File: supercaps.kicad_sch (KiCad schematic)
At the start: 21 parts, among them J30 XT30_F, J31 XT30_F, Q10 2SCR587D3, Q11 2SAR587D3, U18 TLV9301xDBV

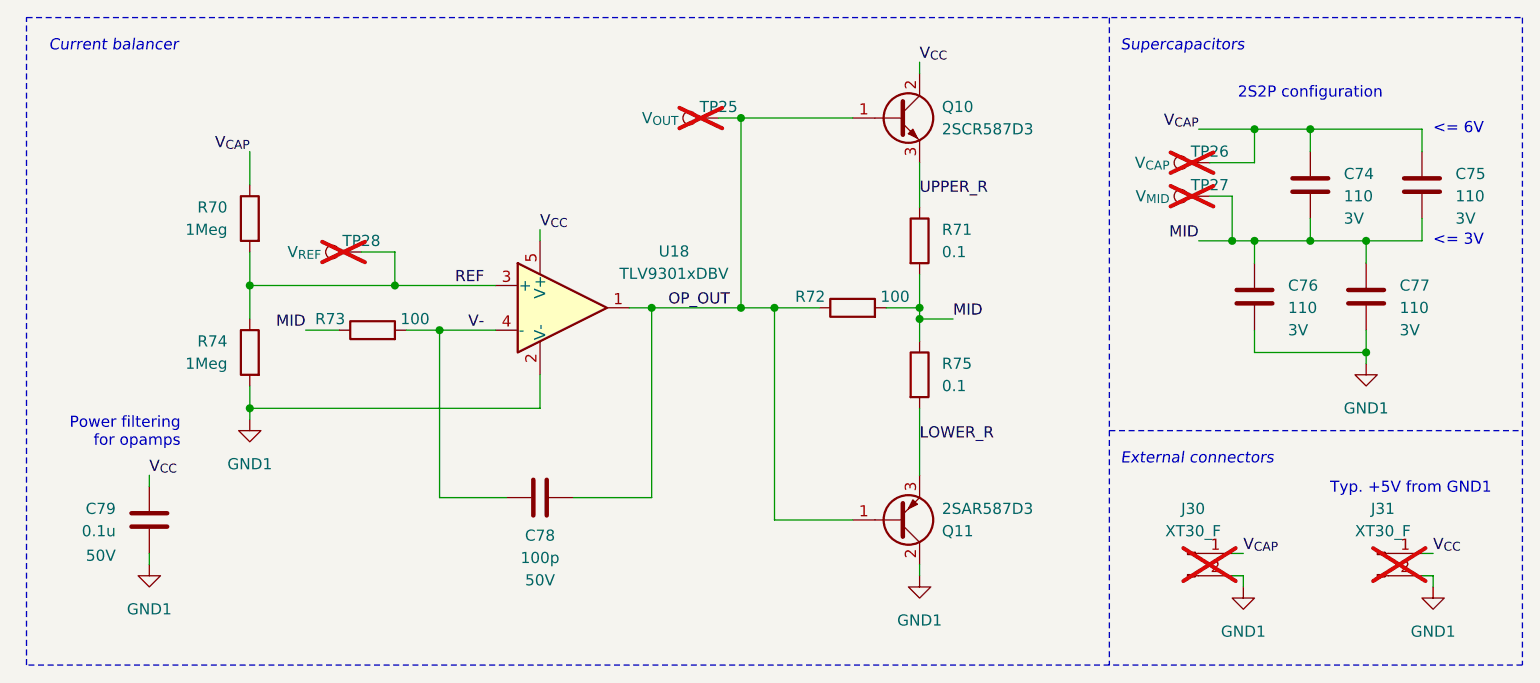
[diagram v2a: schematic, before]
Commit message: Begin layout
Completed ideal diode layout
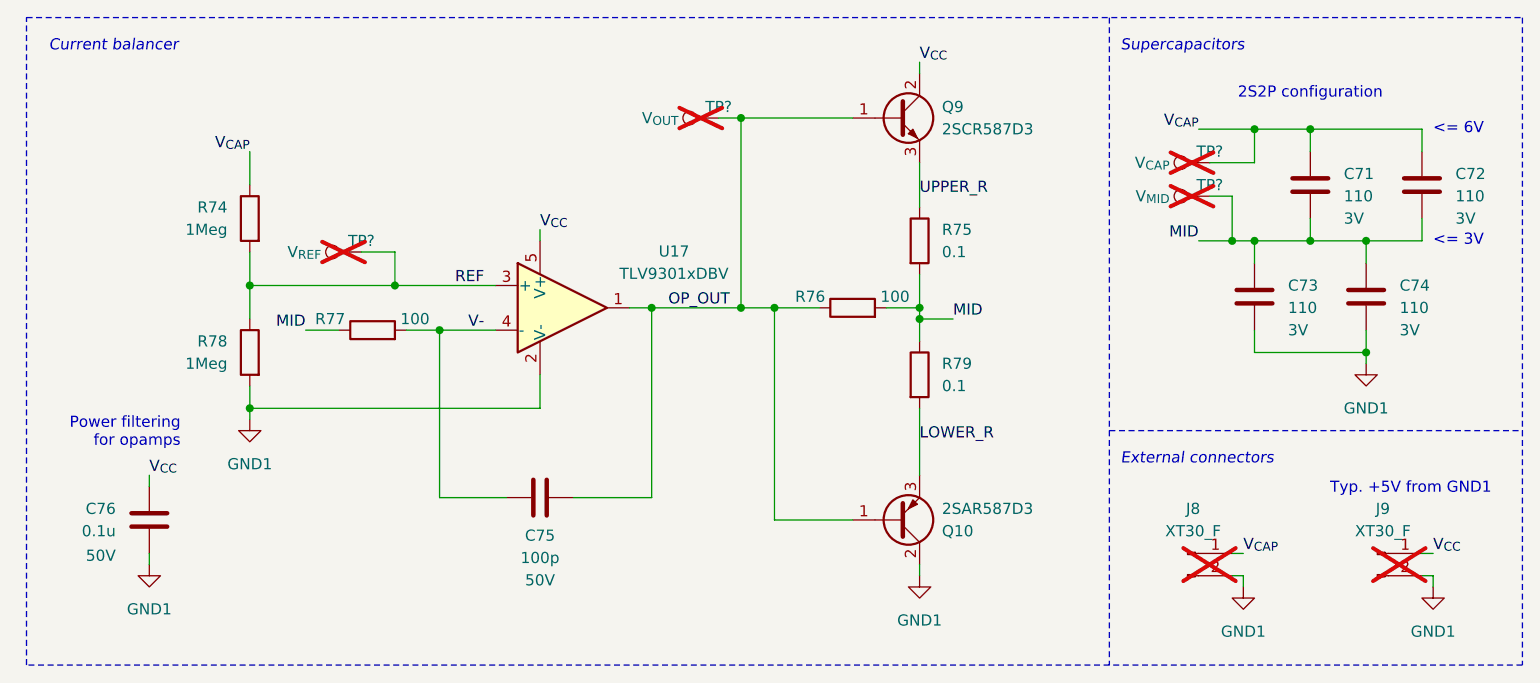
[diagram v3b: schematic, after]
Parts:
- renumbered C74 to C71, C75 to C72, C76 to C73, C77 to C74, C78 to C75, C79 to C76, J30 to J8, J31 to J9, Q11 to Q10, Q10 to Q9, R70 to R74, R71 to R75, R72 to R76, R73 to R77, R74 to R78, R75 to R79, TP28 to TP?, TP25 to TP?, TP26 to TP?, TP27 to TP?, U18 to U17
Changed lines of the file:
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@@
 		(on_board yes)
 		(dnp yes)
-		(property "Reference" "TP28"
+		(property "Reference" "TP?"
 			(at 59.69 50.8 90)
 			(effects
@@
 		)
 		(instances
+			(project "SupercapManager"
+				(path "/6197145b-e7d4-44cc-9d90-537b6501bf60/e69614f9-5cd8-4aa3-ae42-53f80cb78886"
+					(reference "TP?")
+					(unit 1)
+				)
+			)
 			(project "Rev 1B"
 				(path "/e5f99deb-ef42-4c5f-b80a-388477910e20/1165d5b5-e274-4083-890a-7a12aee56ddf"
@@
 		(on_board yes)
 		(dnp no)
-		(property "Reference" "R75"
+		(property "Reference" "R79"
 			(at 125.73 64.7699 0)
 			(effects
@@
 		(on_board yes)
 		(dnp no)
-		(property "Reference" "U18"
+		(property "Reference" "U17"
 			(at 95.25 51.9998 0)
 			(effects
@@
 		(on_board yes)
 		(dnp yes)
-		(property "Reference" "TP25"
+		(property "Reference" "TP?"
 			(at 100.33 35.56 90)
 			(effects
@@
 		)
 		(instances
+			(project "SupercapManager"
+				(path "/6197145b-e7d4-44cc-9d90-537b6501bf60/e69614f9-5cd8-4aa3-ae42-53f80cb78886"
+					(reference "TP?")
+					(unit 1)
+				)
+			)
 			(project "Rev 1B"
 				(path "/e5f99deb-ef42-4c5f-b80a-388477910e20/1165d5b5-e274-4083-890a-7a12aee56ddf"
@@
 		(on_board yes)
 		(dnp no)
-		(property "Reference" "C78"
+		(property "Reference" "C75"
 			(at 80.01 84.328 90)
 			(effects
@@
 		(exclude_from_sim no)
 		(in_bom yes)
-		(on_board no)
+		(on_board yes)
 		(dnp no)
-		(property "Reference" "C76"
+		(property "Reference" "C73"
 			(at 165.1 55.8799 0)
 			(effects
@@
 		(dnp no)
 		(fields_autoplaced yes)
-		(property "Reference" "#PWR0119"
+		(property "Reference" "#PWR098"
 			(at 46.99 77.47 0)
 			(effects
@@
 		(on_board yes)
 		(dnp no)
-		(property "Reference" "C79"
+		(property "Reference" "C76"
 			(at 31.75 81.2799 0)
 			(effects
@@
 		(dnp no)
 		(fields_autoplaced yes)
-		(property "Reference" "#PWR0122"
+		(property "Reference" "#PWR0101"
 			(at 160.02 96.52 0)
 			(effects
@@
 		(on_board yes)
 		(dnp yes)
-		(property "Reference" "J31"
+		(property "Reference" "J9"
 			(at 175.895 81.28 0)
 			(effects
@@
 		(dnp no)
 		(fields_autoplaced yes)
-		(property "Reference" "#PWR0118"
+		(property "Reference" "#PWR097"
 			(at 173.99 71.12 0)
 			(effects
@@
 		(on_board yes)
 		(dnp yes)
-		(property "Reference" "TP26"
+		(property "Reference" "TP?"
 			(at 156.21 40.64 90)
 			(effects
@@
 		)
 		(instances
+			(project "SupercapManager"
+				(path "/6197145b-e7d4-44cc-9d90-537b6501bf60/e69614f9-5cd8-4aa3-ae42-53f80cb78886"
+					(reference "TP?")
+					(unit 1)
+				)
+			)
 			(project "Rev 1B"
 				(path "/e5f99deb-ef42-4c5f-b80a-388477910e20/1165d5b5-e274-4083-890a-7a12aee56ddf"
@@
 		(on_board yes)
 		(dnp no)
-		(property "Reference" "R70"
+		(property "Reference" "R74"
 			(at 44.45 46.9899 0)
 			(effects
@@
 		(exclude_from_sim no)
 		(in_bom yes)
-		(on_board no)
+		(on_board yes)
 		(dnp no)
-		(property "Reference" "C74"
+		(property "Reference" "C71"
 			(at 171.45 43.1799 0)
 			(effects
@@
 		(dnp no)
 		(fields_autoplaced yes)
-		(property "Reference" "#PWR0121"
+		(property "Reference" "#PWR0100"
 			(at 123.19 95.25 0)
 			(effects
@@
 		(on_board yes)
 		(dnp yes)
-		(property "Reference" "J30"
+		(property "Reference" "J8"
 			(at 154.305 81.28 0)
 			(effects
@@
 		(dnp no)
 		(fields_autoplaced yes)
-		(property "Reference" "Q10"
+		(property "Reference" "Q9"
 			(at 125.73 35.5599 0)
 			(effects
@@
 		(on_board yes)
 		(dnp yes)
-		(property "Reference" "TP27"
+		(property "Reference" "TP?"
 			(at 156.21 44.45 90)
 			(effects
@@
 		)
 		(instances
+			(project "SupercapManager"
+				(path "/6197145b-e7d4-44cc-9d90-537b6501bf60/e69614f9-5cd8-4aa3-ae42-53f80cb78886"
+					(reference "TP?")
+					(unit 1)
+				)
+			)
 			(project "Rev 1B"
 				(path "/e5f99deb-ef42-4c5f-b80a-388477910e20/1165d5b5-e274-4083-890a-7a12aee56ddf"
@@
 		(exclude_from_sim no)
 		(in_bom yes)
-		(on_board no)
+		(on_board yes)
 		(dnp no)
-		(property "Reference" "C75"
+		(property "Reference" "C72"
 			(at 184.15 43.1799 0)
 			(effects
@@
 		(on_board yes)
 		(dnp no)
-		(property "Reference" "R71"
+		(property "Reference" "R75"
 			(at 125.73 49.5299 0)
 			(effects
@@
 		(on_board yes)
 		(dnp no)
-		(property "Reference" "R74"
+		(property "Reference" "R78"
 			(at 44.45 62.2299 0)
 			(effects
@@
 		(on_board yes)
 		(dnp no)
-		(property "Reference" "R73"
+		(property "Reference" "R77"
 			(at 56.134 59.69 90)
 			(effects
@@
 		(dnp no)
 		(fields_autoplaced yes)
-		(property "Reference" "#PWR0120"
+		(property "Reference" "#PWR099"
 			(at 35.56 93.98 0)
 			(effects
@@
 		(dnp no)
 		(fields_autoplaced yes)
-		(property "Reference" "#PWR0123"
+		(property "Reference" "#PWR0102"
 			(at 181.61 96.52 0)
 			(effects
@@
 		(on_board yes)
 		(dnp no)
-		(property "Reference" "R72"
+		(property "Reference" "R76"
 			(at 110.744 57.15 90)
 			(effects
@@
 		(on_board yes)
 		(dnp no)
-		(property "Reference" "Q11"
+		(property "Reference" "Q10"
 			(at 125.73 83.8201 0)
 			(effects
@@
 		(exclude_from_sim no)
 		(in_bom yes)
-		(on_board no)
+		(on_board yes)
 		(dnp no)
-		(property "Reference" "C77"
+		(property "Reference" "C74"
 			(at 177.8 55.8799 0)
 			(effects

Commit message: Completed preliminary layout
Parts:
- gave numbers to parts that had none: 4
- renumbered C71 to C74, C72 to C75, C73 to C76, C74 to C77, C75 to C78, C76 to C79, J8 to J30, J9 to J31, Q9 to Q10, Q10 to Q11, R74 to R70, R75 to R71, R76 to R72, R77 to R73, R78 to R74, R79 to R75, U17 to U18
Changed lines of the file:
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@@
 		(on_board yes)
 		(dnp yes)
-		(property "Reference" "TP?"
+		(property "Reference" "TP28"
 			(at 59.69 50.8 90)
 			(effects
@@
 		(on_board yes)
 		(dnp no)
-		(property "Reference" "R79"
+		(property "Reference" "R75"
 			(at 125.73 64.7699 0)
 			(effects
@@
 		(on_board yes)
 		(dnp no)
-		(property "Reference" "U17"
+		(property "Reference" "U18"
 			(at 95.25 51.9998 0)
 			(effects
@@
 		(on_board yes)
 		(dnp yes)
-		(property "Reference" "TP?"
+		(property "Reference" "TP25"
 			(at 100.33 35.56 90)
 			(effects
@@
 		(on_board yes)
 		(dnp no)
-		(property "Reference" "C75"
+		(property "Reference" "C78"
 			(at 80.01 84.328 90)
 			(effects
@@
 		(on_board yes)
 		(dnp no)
-		(property "Reference" "C73"
+		(property "Reference" "C76"
 			(at 165.1 55.8799 0)
 			(effects
@@
 		(dnp no)
 		(fields_autoplaced yes)
-		(property "Reference" "#PWR098"
+		(property "Reference" "#PWR0119"
 			(at 46.99 77.47 0)
 			(effects
@@
 		(on_board yes)
 		(dnp no)
-		(property "Reference" "C76"
+		(property "Reference" "C79"
 			(at 31.75 81.2799 0)
 			(effects
@@
 		(dnp no)
 		(fields_autoplaced yes)
-		(property "Reference" "#PWR0101"
+		(property "Reference" "#PWR0122"
 			(at 160.02 96.52 0)
 			(effects
@@
 		(on_board yes)
 		(dnp yes)
-		(property "Reference" "J9"
+		(property "Reference" "J31"
 			(at 175.895 81.28 0)
 			(effects
@@
 		(dnp no)
 		(fields_autoplaced yes)
-		(property "Reference" "#PWR097"
+		(property "Reference" "#PWR0118"
 			(at 173.99 71.12 0)
 			(effects
@@
 		(on_board yes)
 		(dnp yes)
-		(property "Reference" "TP?"
+		(property "Reference" "TP26"
 			(at 156.21 40.64 90)
 			(effects
@@
 		(on_board yes)
 		(dnp no)
-		(property "Reference" "R74"
+		(property "Reference" "R70"
 			(at 44.45 46.9899 0)
 			(effects
@@
 		(on_board yes)
 		(dnp no)
-		(property "Reference" "C71"
+		(property "Reference" "C74"
 			(at 171.45 43.1799 0)
 			(effects
@@
 		(dnp no)
 		(fields_autoplaced yes)
-		(property "Reference" "#PWR0100"
+		(property "Reference" "#PWR0121"
 			(at 123.19 95.25 0)
 			(effects
@@
 		(on_board yes)
 		(dnp yes)
-		(property "Reference" "J8"
+		(property "Reference" "J30"
 			(at 154.305 81.28 0)
 			(effects
@@
 		(dnp no)
 		(fields_autoplaced yes)
-		(property "Reference" "Q9"
+		(property "Reference" "Q10"
 			(at 125.73 35.5599 0)
 			(effects
@@
 		(on_board yes)
 		(dnp yes)
-		(property "Reference" "TP?"
+		(property "Reference" "TP27"
 			(at 156.21 44.45 90)
 			(effects
@@
 		(on_board yes)
 		(dnp no)
-		(property "Reference" "C72"
+		(property "Reference" "C75"
 			(at 184.15 43.1799 0)
 			(effects
@@
 		(on_board yes)
 		(dnp no)
-		(property "Reference" "R75"
+		(property "Reference" "R71"
 			(at 125.73 49.5299 0)
 			(effects
@@
 		(on_board yes)
 		(dnp no)
-		(property "Reference" "R78"
+		(property "Reference" "R74"
 			(at 44.45 62.2299 0)
 			(effects
@@
 		(on_board yes)
 		(dnp no)
-		(property "Reference" "R77"
+		(property "Reference" "R73"
 			(at 56.134 59.69 90)
 			(effects
@@
 		(dnp no)
 		(fields_autoplaced yes)
-		(property "Reference" "#PWR099"
+		(property "Reference" "#PWR0120"
 			(at 35.56 93.98 0)
 			(effects
@@
 		(dnp no)
 		(fields_autoplaced yes)
-		(property "Reference" "#PWR0102"
+		(property "Reference" "#PWR0123"
 			(at 181.61 96.52 0)
 			(effects
@@
 		(on_board yes)
 		(dnp no)
-		(property "Reference" "R76"
+		(property "Reference" "R72"
 			(at 110.744 57.15 90)
 			(effects
@@
 		(on_board yes)
 		(dnp no)
-		(property "Reference" "Q10"
+		(property "Reference" "Q11"
 			(at 125.73 83.8201 0)
 			(effects
@@
 		(on_board yes)
 		(dnp no)
-		(property "Reference" "C74"
+		(property "Reference" "C77"
 			(at 177.8 55.8799 0)
 			(effects

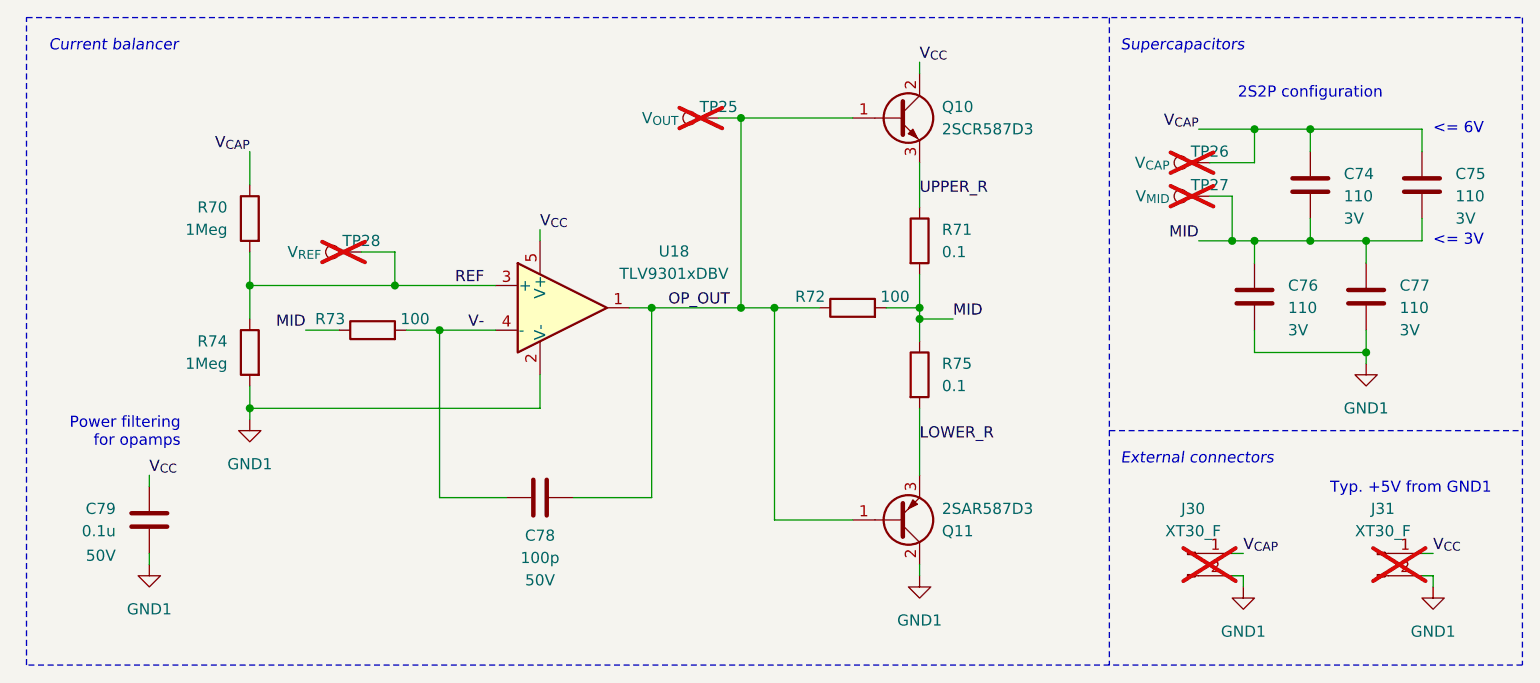
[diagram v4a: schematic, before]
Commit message: Placed footprints for boost stage 1 layout
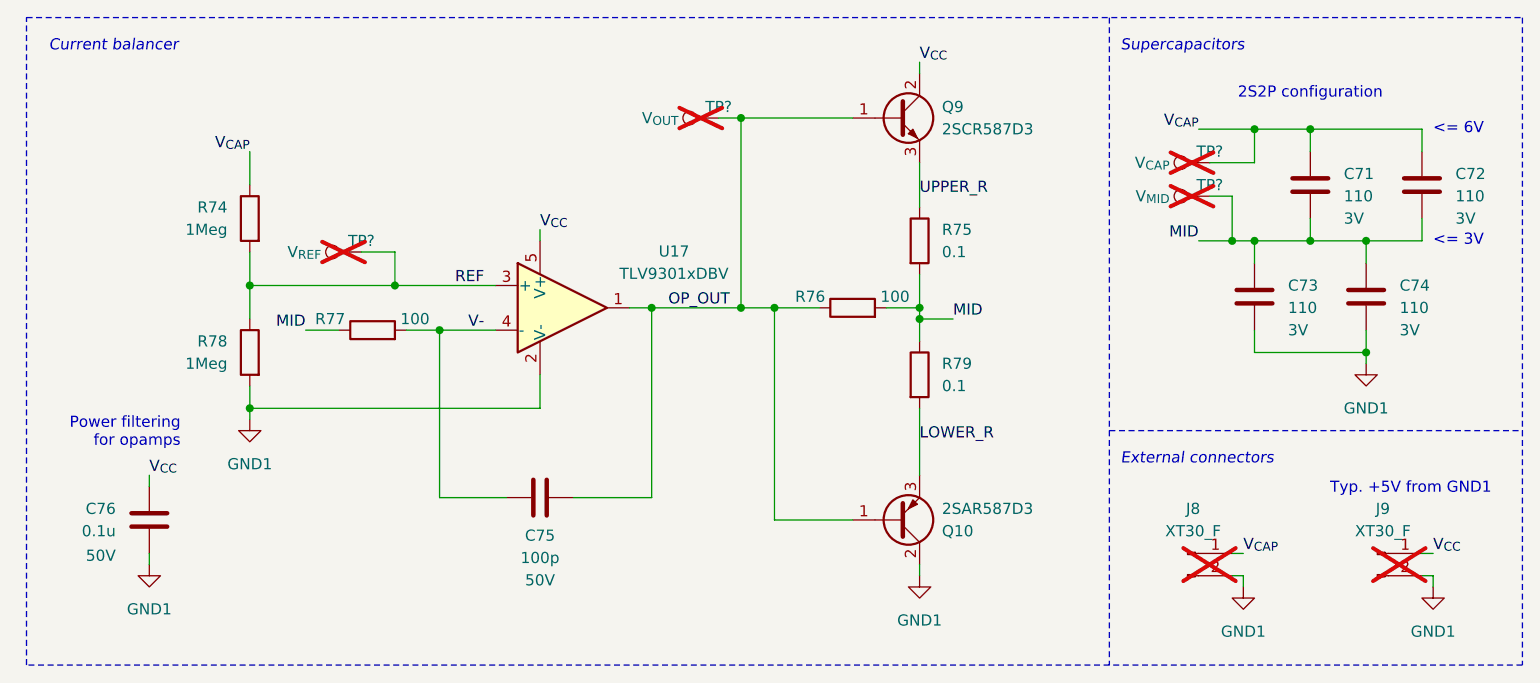
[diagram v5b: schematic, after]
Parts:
- renumbered C74 to C71, C75 to C72, C76 to C73, C77 to C74, C78 to C75, C79 to C76, J30 to J8, J31 to J9, Q11 to Q10, Q10 to Q9, R70 to R74, R71 to R75, R72 to R76, R73 to R77, R74 to R78, R75 to R79, TP28 to TP?, TP25 to TP?, TP26 to TP?, TP27 to TP?, U18 to U17
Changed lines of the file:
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@@
 		(on_board yes)
 		(dnp yes)
-		(property "Reference" "TP28"
+		(property "Reference" "TP?"
 			(at 59.69 50.8 90)
 			(effects
@@
 		(on_board yes)
 		(dnp no)
-		(property "Reference" "R75"
+		(property "Reference" "R79"
 			(at 125.73 64.7699 0)
 			(effects
@@
 		(on_board yes)
 		(dnp no)
-		(property "Reference" "U18"
+		(property "Reference" "U17"
 			(at 95.25 51.9998 0)
 			(effects
@@
 		(on_board yes)
 		(dnp yes)
-		(property "Reference" "TP25"
+		(property "Reference" "TP?"
 			(at 100.33 35.56 90)
 			(effects
@@
 		(on_board yes)
 		(dnp no)
-		(property "Reference" "C78"
+		(property "Reference" "C75"
 			(at 80.01 84.328 90)
 			(effects
@@
 		(on_board yes)
 		(dnp no)
-		(property "Reference" "C76"
+		(property "Reference" "C73"
 			(at 165.1 55.8799 0)
 			(effects
@@
 		(dnp no)
 		(fields_autoplaced yes)
-		(property "Reference" "#PWR0119"
+		(property "Reference" "#PWR098"
 			(at 46.99 77.47 0)
 			(effects
@@
 		(on_board yes)
 		(dnp no)
-		(property "Reference" "C79"
+		(property "Reference" "C76"
 			(at 31.75 81.2799 0)
 			(effects
@@
 		(dnp no)
 		(fields_autoplaced yes)
-		(property "Reference" "#PWR0122"
+		(property "Reference" "#PWR0101"
 			(at 160.02 96.52 0)
 			(effects
@@
 		(on_board yes)
 		(dnp yes)
-		(property "Reference" "J31"
+		(property "Reference" "J9"
 			(at 175.895 81.28 0)
 			(effects
@@
 		(dnp no)
 		(fields_autoplaced yes)
-		(property "Reference" "#PWR0118"
+		(property "Reference" "#PWR097"
 			(at 173.99 71.12 0)
 			(effects
@@
 		(on_board yes)
 		(dnp yes)
-		(property "Reference" "TP26"
+		(property "Reference" "TP?"
 			(at 156.21 40.64 90)
 			(effects
@@
 		(on_board yes)
 		(dnp no)
-		(property "Reference" "R70"
+		(property "Reference" "R74"
 			(at 44.45 46.9899 0)
 			(effects
@@
 		(on_board yes)
 		(dnp no)
-		(property "Reference" "C74"
+		(property "Reference" "C71"
 			(at 171.45 43.1799 0)
 			(effects
@@
 		(dnp no)
 		(fields_autoplaced yes)
-		(property "Reference" "#PWR0121"
+		(property "Reference" "#PWR0100"
 			(at 123.19 95.25 0)
 			(effects
@@
 		(on_board yes)
 		(dnp yes)
-		(property "Reference" "J30"
+		(property "Reference" "J8"
 			(at 154.305 81.28 0)
 			(effects
@@
 		(dnp no)
 		(fields_autoplaced yes)
-		(property "Reference" "Q10"
+		(property "Reference" "Q9"
 			(at 125.73 35.5599 0)
 			(effects
@@
 		(on_board yes)
 		(dnp yes)
-		(property "Reference" "TP27"
+		(property "Reference" "TP?"
 			(at 156.21 44.45 90)
 			(effects
@@
 		(on_board yes)
 		(dnp no)
-		(property "Reference" "C75"
+		(property "Reference" "C72"
 			(at 184.15 43.1799 0)
 			(effects
@@
 		(on_board yes)
 		(dnp no)
-		(property "Reference" "R71"
+		(property "Reference" "R75"
 			(at 125.73 49.5299 0)
 			(effects
@@
 		(on_board yes)
 		(dnp no)
-		(property "Reference" "R74"
+		(property "Reference" "R78"
 			(at 44.45 62.2299 0)
 			(effects
@@
 		(on_board yes)
 		(dnp no)
-		(property "Reference" "R73"
+		(property "Reference" "R77"
 			(at 56.134 59.69 90)
 			(effects
@@
 		(dnp no)
 		(fields_autoplaced yes)
-		(property "Reference" "#PWR0120"
+		(property "Reference" "#PWR099"
 			(at 35.56 93.98 0)
 			(effects
@@
 		(dnp no)
 		(fields_autoplaced yes)
-		(property "Reference" "#PWR0123"
+		(property "Reference" "#PWR0102"
 			(at 181.61 96.52 0)
 			(effects
@@
 		(on_board yes)
 		(dnp no)
-		(property "Reference" "R72"
+		(property "Reference" "R76"
 			(at 110.744 57.15 90)
 			(effects
@@
 		(on_board yes)
 		(dnp no)
-		(property "Reference" "Q11"
+		(property "Reference" "Q10"
 			(at 125.73 83.8201 0)
 			(effects
@@
 		(on_board yes)
 		(dnp no)
-		(property "Reference" "C77"
+		(property "Reference" "C74"
 			(at 177.8 55.8799 0)
 			(effects
